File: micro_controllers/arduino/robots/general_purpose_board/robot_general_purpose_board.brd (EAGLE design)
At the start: 100 x 80 mm, 46 parts, among them IC1 ATMEGA328, IC2 7805, IC3 L293D, IC4 358, IC5 358, Q1 16MHZ

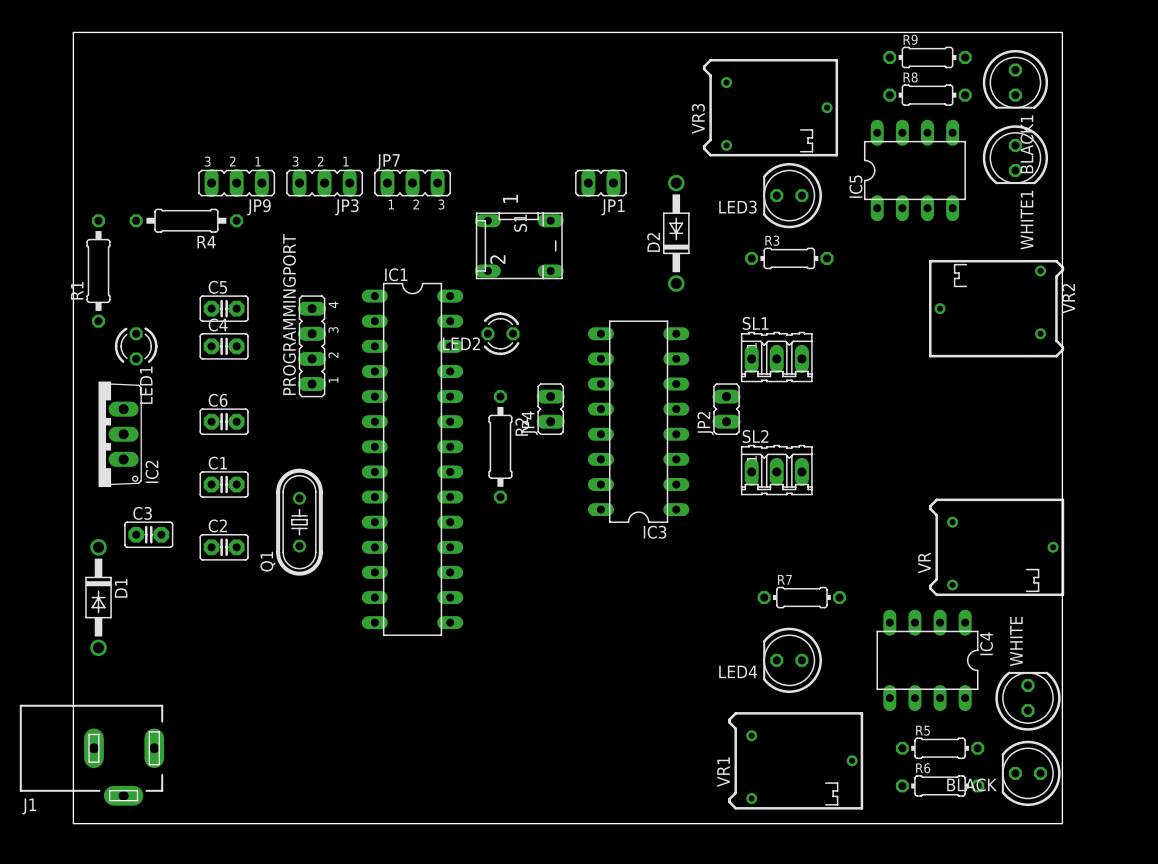
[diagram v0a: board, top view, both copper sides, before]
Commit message: 
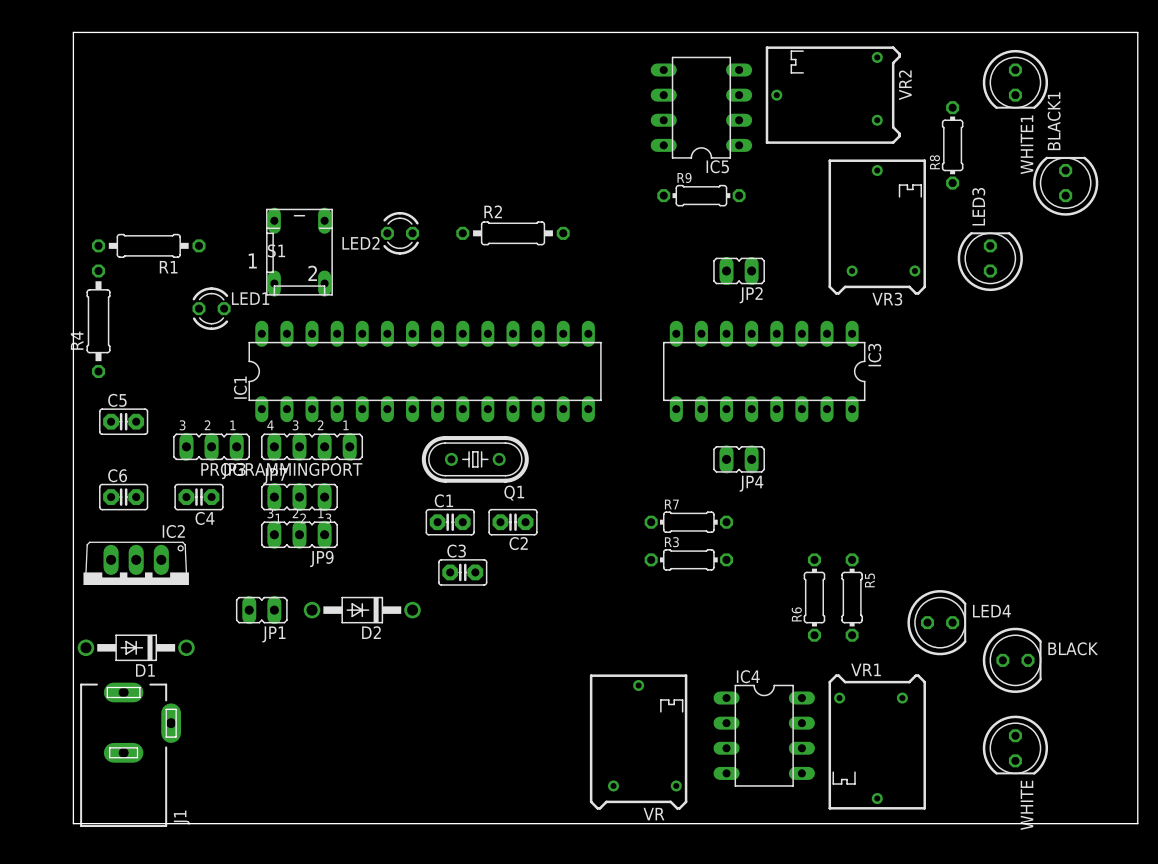
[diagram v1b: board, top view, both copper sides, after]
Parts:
- removed SL1, SL2: (no value), con-amp-quick:03P
- moved JP1 55.1 mm to (19.1, 20.3)
- moved D2 49.6 mm to (29.2, 20.3), turned to 180 degrees
- moved VR 40.5 mm to (57.1, 5.08), turned to 90 degrees
- moved JP9 36.1 mm to (22.9, 27.9)
- moved JP7 33.7 mm to (22.9, 31.8)
- moved R3 32.1 mm to (62.2, 25.4)
- moved C3 32.0 mm to (39.4, 24.1)
- moved C2 29.3 mm to (44.5, 29.2), turned to 180 degrees
- moved JP3 29.0 mm to (14.0, 36.8)
- moved VR2 27.2 mm to (78.7, 72.4)
- moved R9 26.8 mm to (63.5, 62.2)
- moved C1 23.2 mm to (38.1, 29.2)
- moved R6 22.9 mm to (74.9, 21.6), turned to 90 degrees
- moved IC5 22.5 mm to (63.5, 71.1), turned to 90 degrees
- moved R2 21.6 mm to (44.5, 58.4), turned to 0 degrees
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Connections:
- removed net N$4: C4.1
- net +12V: now also C4.1
- net +5V: no longer SL1.1, SL2.1
- net GND: no longer SL1.3, SL2.3
- net N$20: no longer SL1.2
- net N$34: no longer SL2.2
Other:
- board size 100 x 80 mm -> 107.6 x 80 mm

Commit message: 
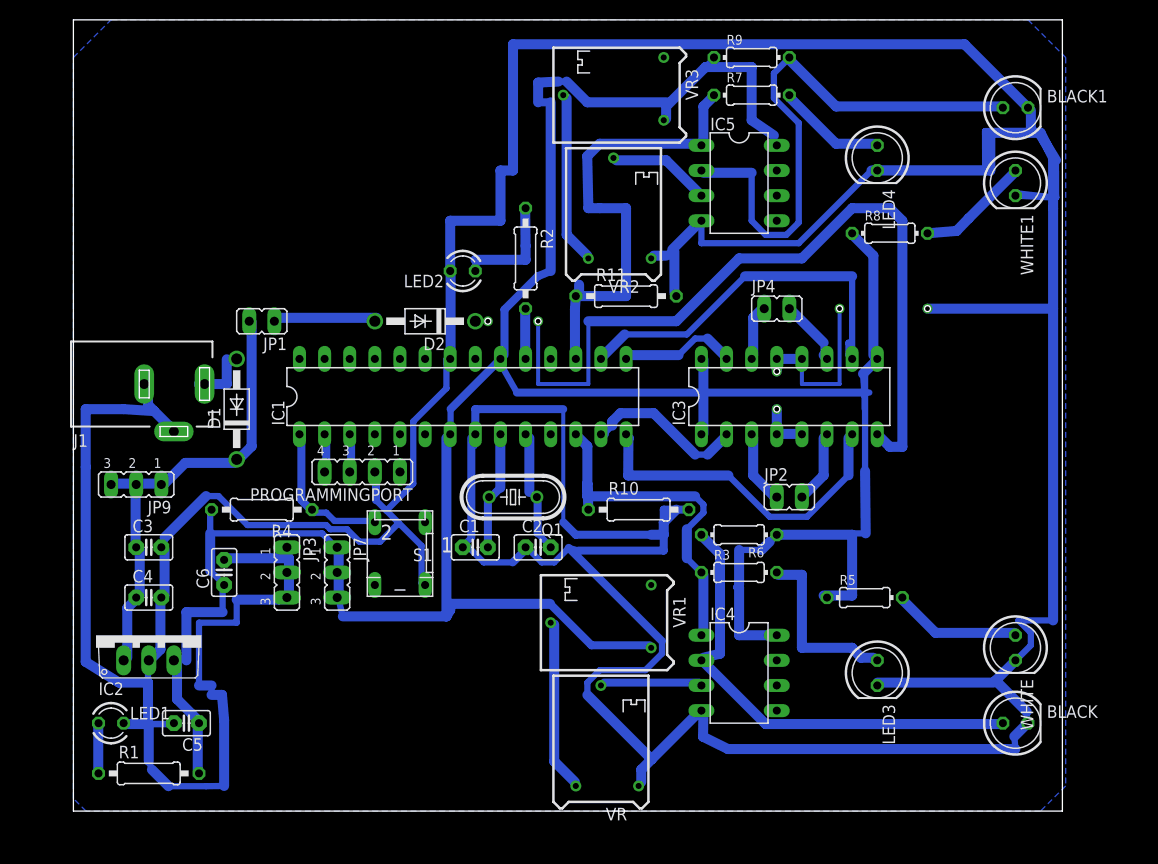
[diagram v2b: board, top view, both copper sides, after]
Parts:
- added R10, R11: 10K, rcl:0207/10
- C3: value 100UF -> 470Uf
- moved R1 53.3 mm to (7.62, 3.81), turned to 0 degrees
- moved LED4 47.4 mm to (81.3, 66.0), turned to 270 degrees
- moved R7 43.6 mm to (68.6, 72.4)
- moved LED3 43.4 mm to (81.3, 14.0), turned to 270 degrees
- moved LED1 43.1 mm to (3.81, 8.89)
- moved J1 34.7 mm to (10.2, 43.2), turned to 270 degrees
- moved C3 31.9 mm to (7.62, 26.7)
- moved C5 31.1 mm to (11.4, 8.89), turned to 180 degrees
- moved S1 30.9 mm to (33.0, 26.7), turned to 180 degrees
- moved D2 29.9 mm to (35.6, 49.5)
- moved JP1 29.2 mm to (19.1, 49.5)
- moved VR3 28.5 mm to (57.1, 72.4), turned to 180 degrees
- moved VR2 27.9 mm to (54.6, 58.4), turned to 90 degrees
- moved VR1 27.4 mm to (55.9, 19.1), turned to 180 degrees
- moved D1 26.2 mm to (16.5, 40.6), turned to 90 degrees
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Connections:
- removed net N$34: IC1.14, IC5.1, R7.1
- new net N$33: IC1.13, IC3.2
- net GND: now also R10.2, R11.2
- net N$20: now also IC1.12, R10.1; no longer IC1.13
- net N$25: now also IC1.14; no longer IC1.17
- net N$26: now also IC1.17, IC5.1, R11.1, R7.1; no longer IC1.18, IC3.2
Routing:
- net GND: track 0.00 -> 671.0 mm, vias 0 -> 3
- net +5V: track 0.00 -> 314.0 mm
- net N$7: track 0.00 -> 82.0 mm, vias 0 -> 2
- net N$36: track 0.00 -> 58.1 mm
- net N$26: track 0.00 -> 48.4 mm
- net N$22: track 0.00 -> 48.0 mm
- net +12V: track 0.00 -> 47.5 mm
- net N$24: track 0.00 -> 40.7 mm
- net N$20: track 0.00 -> 36.1 mm
- net N$25: track 0.00 -> 34.3 mm
- net N$32: track 0.00 -> 18.2 mm
- net N$29: track 0.00 -> 17.6 mm
- net N$38: track 0.00 -> 17.5 mm
- net N$33: track 0.00 -> 16.5 mm
- net N$31: track 0.00 -> 15.1 mm
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- added copper zone on layer 16, net N$34
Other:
- board size 107.6 x 80 mm -> 100 x 80 mm

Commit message: 
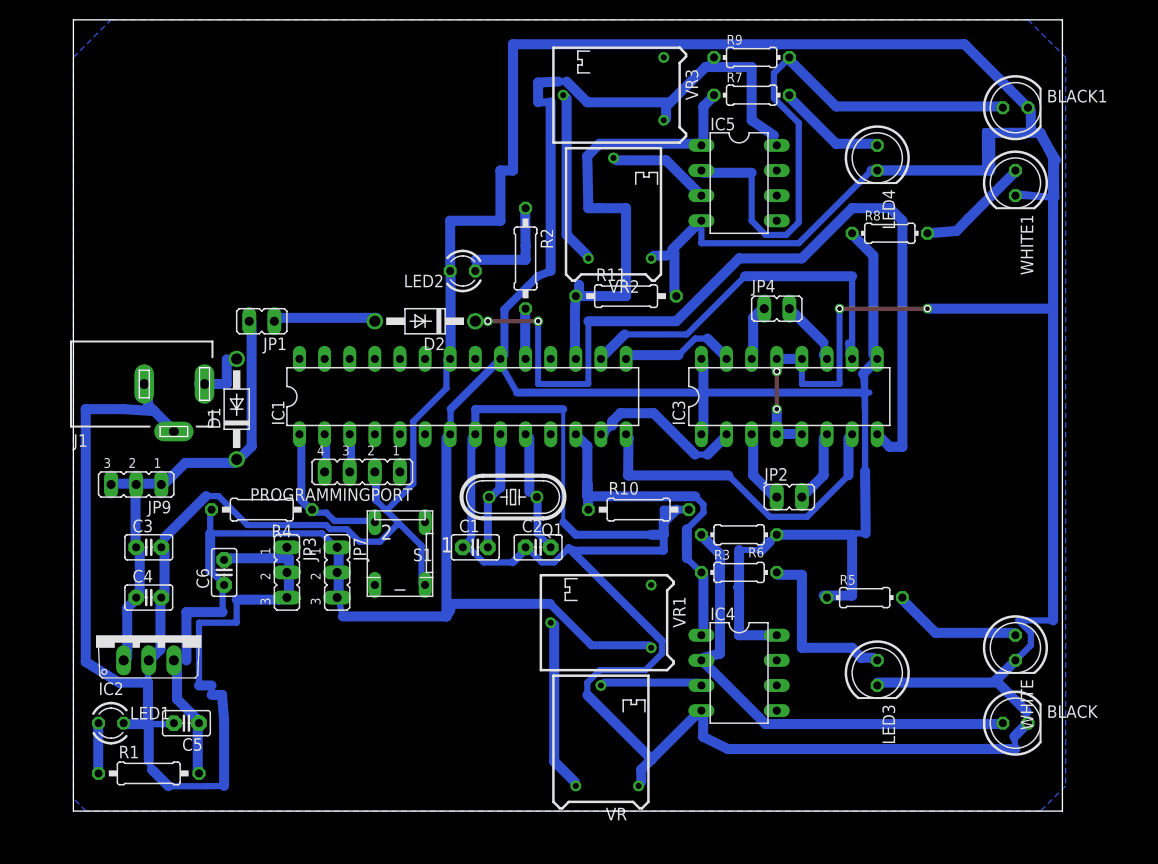
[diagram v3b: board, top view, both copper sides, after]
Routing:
- net GND: track 671.0 -> 683.7 mm
- net N$7: track 82.0 -> 87.1 mm
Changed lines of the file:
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@@
 <grid distance="0.05" unitdist="inch" unit="inch" style="lines" multiple="1" display="no" altdistance="0.025" altunitdist="inch" altunit="inch"/>
 <layers>
-<layer number="1" name="Top" color="4" fill="1" visible="yes" active="yes"/>
+<layer number="1" name="Top" color="4" fill="1" visible="no" active="yes"/>
 <layer number="16" name="Bottom" color="1" fill="1" visible="yes" active="yes"/>
 <layer number="17" name="Pads" color="2" fill="1" visible="yes" active="yes"/>
 <layer number="18" name="Vias" color="2" fill="1" visible="yes" active="yes"/>
-<layer number="19" name="Unrouted" color="6" fill="1" visible="yes" active="yes"/>
+<layer number="19" name="Unrouted" color="6" fill="1" visible="no" active="yes"/>
 <layer number="20" name="Dimension" color="15" fill="1" visible="yes" active="yes"/>
-<layer number="21" name="tPlace" color="7" fill="1" visible="yes" active="yes"/>
-<layer number="22" name="bPlace" color="7" fill="1" visible="yes" active="yes"/>
-<layer number="23" name="tOrigins" color="15" fill="1" visible="yes" active="yes"/>
-<layer number="24" name="bOrigins" color="15" fill="1" visible="yes" active="yes"/>
-<layer number="25" name="tNames" color="7" fill="1" visible="yes" active="yes"/>
-<layer number="26" name="bNames" color="7" fill="1" visible="yes" active="yes"/>
-<layer number="27" name="tValues" color="7" fill="1" visible="yes" active="yes"/>
-<layer number="28" name="bValues" color="7" fill="1" visible="yes" active="yes"/>
+<layer number="21" name="tPlace" color="7" fill="1" visible="no" active="yes"/>
+<layer number="22" name="bPlace" color="7" fill="1" visible="no" active="yes"/>
+<layer number="23" name="tOrigins" color="15" fill="1" visible="no" active="yes"/>
+<layer number="24" name="bOrigins" color="15" fill="1" visible="no" active="yes"/>
+<layer number="25" name="tNames" color="7" fill="1" visible="no" active="yes"/>
+<layer number="26" name="bNames" color="7" fill="1" visible="no" active="yes"/>
+<layer number="27" name="tValues" color="7" fill="1" visible="no" active="yes"/>
+<layer number="28" name="bValues" color="7" fill="1" visible="no" active="yes"/>
 <layer number="29" name="tStop" color="7" fill="3" visible="no" active="yes"/>
 <layer number="30" name="bStop" color="7" fill="6" visible="no" active="yes"/>
@@
 <layer number="37" name="tTest" color="7" fill="1" visible="no" active="yes"/>
 <layer number="38" name="bTest" color="7" fill="1" visible="no" active="yes"/>
-<layer number="39" name="tKeepout" color="4" fill="11" visible="yes" active="yes"/>
-<layer number="40" name="bKeepout" color="1" fill="11" visible="yes" active="yes"/>
-<layer number="41" name="tRestrict" color="4" fill="10" visible="yes" active="yes"/>
-<layer number="42" name="bRestrict" color="1" fill="10" visible="yes" active="yes"/>
-<layer number="43" name="vRestrict" color="2" fill="10" visible="yes" active="yes"/>
+<layer number="39" name="tKeepout" color="4" fill="11" visible="no" active="yes"/>
+<layer number="40" name="bKeepout" color="1" fill="11" visible="no" active="yes"/>
+<layer number="41" name="tRestrict" color="4" fill="10" visible="no" active="yes"/>
+<layer number="42" name="bRestrict" color="1" fill="10" visible="no" active="yes"/>
+<layer number="43" name="vRestrict" color="2" fill="10" visible="no" active="yes"/>
 <layer number="44" name="Drills" color="7" fill="1" visible="no" active="yes"/>
-<layer number="45" name="Holes" color="7" fill="1" visible="yes" active="yes"/>
+<layer number="45" name="Holes" color="7" fill="1" visible="no" active="yes"/>
 <layer number="46" name="Milling" color="3" fill="1" visible="no" active="yes"/>
 <layer number="47" name="Measures" color="7" fill="1" visible="no" active="yes"/>
-<layer number="48" name="Document" color="7" fill="1" visible="yes" active="yes"/>
-<layer number="49" name="Reference" color="7" fill="1" visible="yes" active="yes"/>
-<layer number="51" name="tDocu" color="7" fill="1" visible="yes" active="yes"/>
-<layer number="52" name="bDocu" color="7" fill="1" visible="yes" active="yes"/>
+<layer number="48" name="Document" color="7" fill="1" visible="no" active="yes"/>
+<layer number="49" name="Reference" color="7" fill="1" visible="no" active="yes"/>
+<layer number="51" name="tDocu" color="7" fill="1" visible="no" active="yes"/>
+<layer number="52" name="bDocu" color="7" fill="1" visible="no" active="yes"/>
 <layer number="53" name="tGND_GNDA" color="7" fill="9" visible="no" active="no"/>
 <layer number="54" name="bGND_GNDA" color="1" fill="9" visible="no" active="no"/>
@@
 <wire x1="8.8011" y1="21.3741" x2="8.89" y2="21.59" width="0.635" layer="16"/>
 <wire x1="7.9629" y1="15.5067" x2="7.62" y2="15.24" width="0.635" layer="16"/>
-<wire x1="1.2446" y1="34.7853" x2="1.2446" y2="40.64" width="1.016" layer="16"/>
 <wire x1="1.2446" y1="40.64" x2="5.08" y2="40.64" width="1.016" layer="16"/>
 <wire x1="5.08" y1="40.64" x2="8.17245" y2="40.44315" width="1.016" layer="16"/>
-<wire x1="1.2446" y1="15.0876" x2="1.2446" y2="34.7853" width="1.016" layer="16"/>
+<wire x1="1.2446" y1="15.0876" x2="1.2446" y2="40.64" width="1.016" layer="16"/>
 <wire x1="4.6101" y1="12.9921" x2="1.2446" y2="15.0876" width="1.016" layer="16"/>
 <wire x1="7.5438" y1="12.9921" x2="4.6101" y2="12.9921" width="1.016" layer="16"/>
@@
 <wire x1="40.64" y1="40.64" x2="40.64" y2="38.1" width="0.8128" layer="16"/>
 <wire x1="40.64" y1="36.83" x2="40.64" y2="38.1" width="0.4064" layer="16"/>
-<wire x1="73.66" y1="43.18" x2="77.47" y2="43.18" width="0.4064" layer="16"/>
-<wire x1="77.47" y1="43.18" x2="77.47" y2="50.8" width="0.4064" layer="16"/>
+<wire x1="73.66" y1="43.18" x2="77.47" y2="43.18" width="0.6096" layer="16"/>
+<wire x1="77.47" y1="43.18" x2="77.47" y2="50.8" width="0.6096" layer="16"/>
 <wire x1="71.247" y1="38.1381" x2="71.12" y2="38.2651" width="0.4064" layer="16" curve="-90"/>
 <wire x1="71.12" y1="38.2651" x2="71.12" y2="40.64" width="1.016" layer="16"/>
-<wire x1="73.66" y1="43.18" x2="73.66" y2="45.72" width="0.4064" layer="16"/>
+<wire x1="73.66" y1="43.18" x2="73.66" y2="45.72" width="0.6096" layer="16"/>
 <wire x1="73.66" y1="45.72" x2="71.12" y2="45.72" width="1.016" layer="16"/>
 <wire x1="71.12" y1="45.72" x2="71.12" y2="44.45" width="1.016" layer="16"/>
@@
 <wire x1="99.06" y1="60.96" x2="99.06" y2="50.8" width="0.4064" layer="16"/>
 <wire x1="99.06" y1="50.8" x2="86.36" y2="50.8" width="1.016" layer="16"/>
-<wire x1="71.12" y1="40.64" x2="73.66" y2="43.18" width="0" layer="19" extent="16-16"/>
-<wire x1="73.3425" y1="57.4167" x2="77.47" y2="50.8" width="0" layer="19" extent="16-16"/>
+<wire x1="71.12" y1="40.64" x2="71.12" y2="44.45" width="0.4064" layer="1"/>
+<wire x1="77.47" y1="50.8" x2="86.36" y2="50.8" width="0.4064" layer="1"/>
+<wire x1="86.36" y1="50.8" x2="86.36" y2="50.8" width="0" layer="19" extent="1-16"/>
 </signal>
 <signal name="N$5">
@@
 <wire x1="67.31" y1="55.88" x2="60.96" y2="49.53" width="1.016" layer="16"/>
 <wire x1="60.96" y1="49.53" x2="52.07" y2="49.53" width="1.016" layer="16"/>
-<wire x1="52.07" y1="49.53" x2="52.07" y2="43.18" width="0.4064" layer="16"/>
-<wire x1="52.07" y1="43.18" x2="46.99" y2="43.18" width="0.4064" layer="16"/>
-<wire x1="46.99" y1="43.18" x2="46.99" y2="49.53" width="0.4064" layer="16"/>
+<wire x1="52.07" y1="49.53" x2="52.07" y2="43.18" width="0.6096" layer="16"/>
+<wire x1="52.07" y1="43.18" x2="46.99" y2="43.18" width="0.6096" layer="16"/>
+<wire x1="46.99" y1="43.18" x2="46.99" y2="49.53" width="0.6096" layer="16"/>
 <wire x1="40.64" y1="49.53" x2="41.91" y2="49.53" width="0.4064" layer="16"/>
 <via x="41.91" y="49.53" extent="1-16" drill="0.6" shape="square"/>
 <via x="46.99" y="49.53" extent="1-16" drill="0.6" shape="square"/>
-<wire x1="41.91" y1="49.53" x2="46.99" y2="49.53" width="0" layer="19" extent="16-16"/>
+<wire x1="46.99" y1="49.53" x2="41.91" y2="49.53" width="0.4064" layer="1"/>
 </signal>
 <signal name="N$14">
